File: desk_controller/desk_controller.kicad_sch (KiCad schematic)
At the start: 25 parts

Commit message: Some work
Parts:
- removed J?: RJ12, symbol Connector:RJ12
- added J?: UART2_header, Connector_PinHeader_2.54mm:PinHeader_1x04_P2.54mm_Vertical, symbol Connector_Generic:Conn_01x04
- added J?: RJ45, symbol Connector:RJ45
- added R? (x6): R, symbol Device:R
- added U? (x4): PC817, Package_DIP:DIP-4_W7.62mm, symbol Isolator:PC817
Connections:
- net +3V3: now also J?.1 (Pin_1), U?.4
- net GND: now also J?.4 (Pin_4), R?.1, R?.1, U?.2, U?.2, U?.2, U?.2
- net MISO: no longer names the net of U?.12 (PA6)
- net MOSI: no longer names the net of U?.13 (PA7)
- net NAND_CS: no longer names the net of U?.10 (PA4)
- net PA0: no longer names the net of U?.6 (PA0)
- net PA1: no longer names the net of U?.7 (PA1)
- net PA11: no longer names the net of U?.21 (PA11)
- net PA12: no longer names the net of U?.22 (PA12)
- net PA15: no longer names the net of U?.25 (PA15)
- net PA2: no longer names the net of U?.8 (PA2)
- net PA3: no longer names the net of U?.9 (PA3)
- net PA8: no longer names the net of U?.18 (PA8)
- net PB0: no longer names the net of U?.14 (PB0)
- net PB1: no longer names the net of U?.15 (PB1)
- net PB3: no longer names the net of U?.26 (PB3)
- net PB4: no longer names the net of U?.27 (PB4)
- net PB5: no longer names the net of U?.28 (PB5)
- net PB6: no longer names the net of U?.29 (PB6)
- net PB7: no longer names the net of U?.30 (PB7)
- net SCK: no longer names the net of U?.11 (PA5)
- new net: R?.2, U?.1 (x4)
- new net 232_RX: R?.1
- new net 232_RX_ISOLATED: R?.2, U?.3
- new net 232_TX: R?.1
- new net 232_TX_ISOLATED: R?.2, U?.3
- new net POWER_SIG: R?.1
- new net RESET_SIG: R?.1
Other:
- note added: "MJ3215-88-1-2-N"
- note added: "optos are APC-817D1-SL"
- company: (none) -> Stefano Nicolis
- title: (none) -> Desk Controller
- moved on the sheet: C?, D?, J?, PS?, Q?, R?, RV?, SW?, U?

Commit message: Sch work
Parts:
- added C?: 10u, symbol Device:C_Polarized
- added D?: D_Schottky, symbol Device:D_Schottky
- added R?: R, symbol Device:R
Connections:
- net 232_RX: now also J?.6
- net 232_TX: now also J?.5
- net GND: now also J?.8, C?.2
- net VBUS: now reaches U?.4
- net VBUS: now also C?.1, R?.1
- net POWER-: now reaches U?.3
- net POWER-: now also J?.2
- net POWER+: now reaches U?.4
- net POWER+: now also J?.1
- net RESET-: now reaches U?.3
- net RESET-: now also J?.4
- net RESET+: now reaches U?.4
- net RESET+: now also J?.3
- net 232_DTR: now reaches J?.7
- net 232_DTR: now also D?.2 (A)
- new net: D?.1 (K), R?.2
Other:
- moved on the sheet: C?, D?, J?, PS?, Q?, R?, RV?, SW?, U?

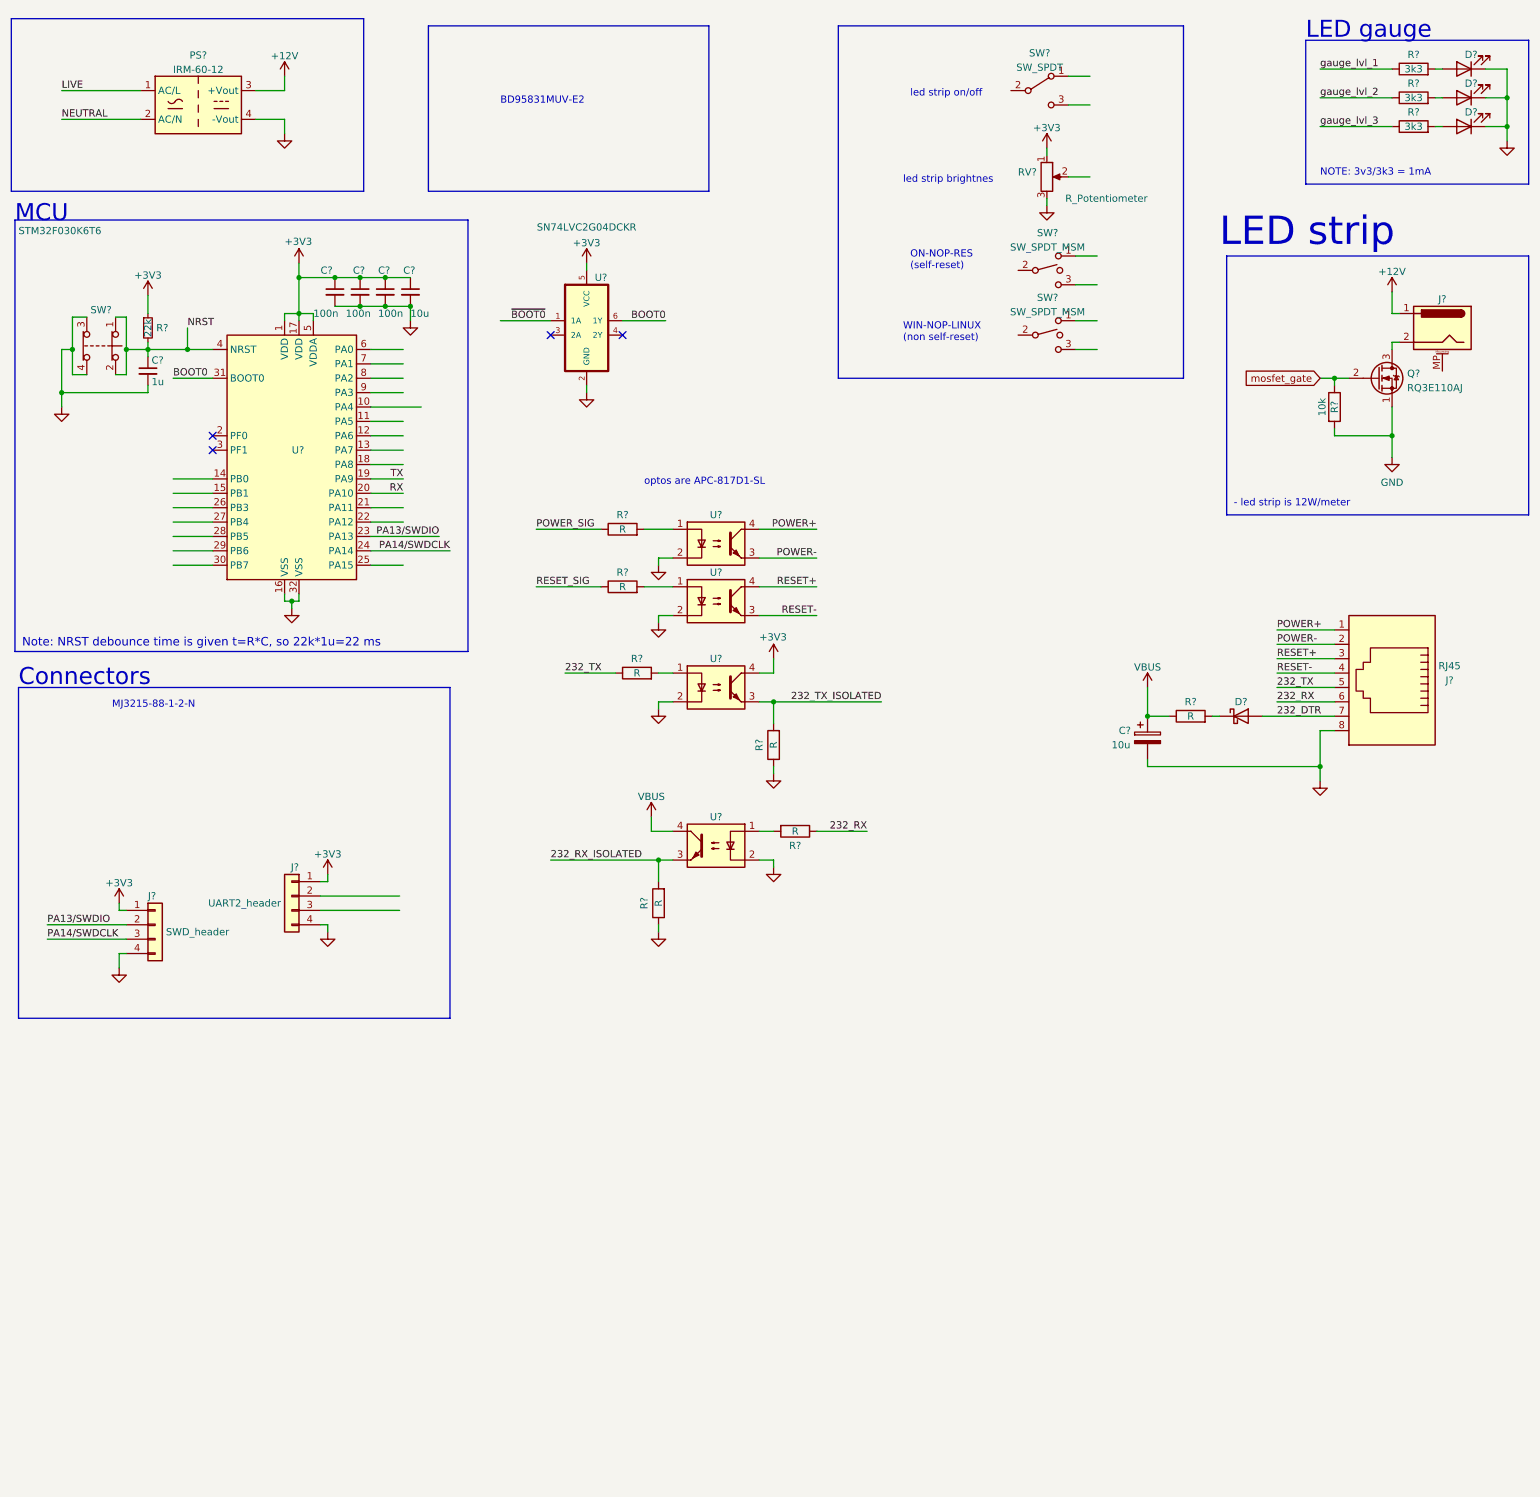
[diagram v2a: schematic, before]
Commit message: Added sheets in sch, added TI document for isolated rs232 interface with power harvesting, general sch work
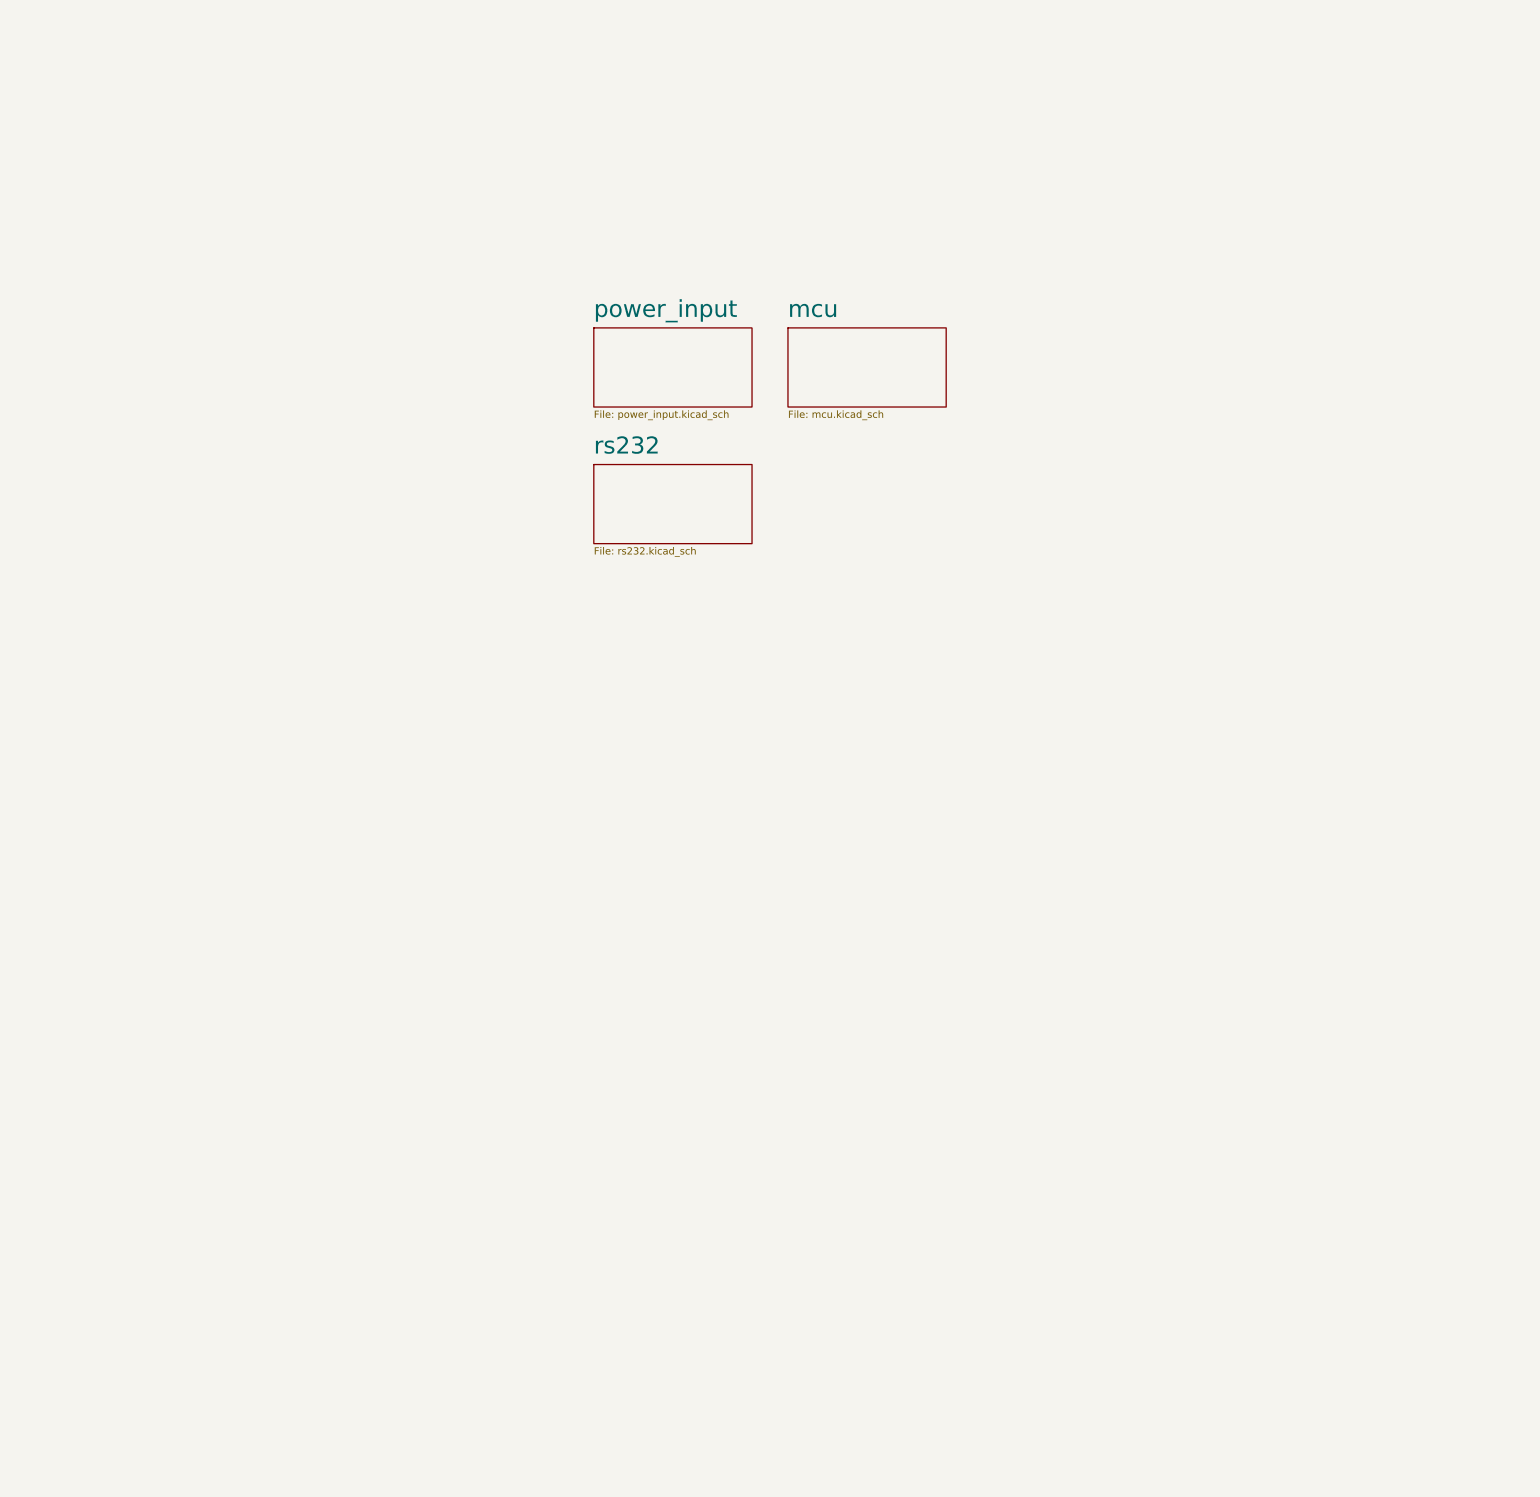
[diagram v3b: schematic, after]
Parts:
- removed C?: 1u, Capacitor_SMD:C_0603_1608Metric, symbol Device:C_Small
- removed C? (x3): 100n, Capacitor_SMD:C_0603_1608Metric, symbol Device:C_Small
- removed C?: 10u, symbol Device:C_Polarized
- removed C?: 10u, Capacitor_SMD:C_0603_1608Metric, symbol Device:C_Small
- removed D?: GREEN, LED_SMD:LED_0603_1608Metric, symbol Device:LED
- removed D? (x2): RED, LED_SMD:LED_0603_1608Metric, symbol Device:LED
- removed D?: D_Schottky, symbol Device:D_Schottky
- removed J?: UART2_header, Connector_PinHeader_2.54mm:PinHeader_1x04_P2.54mm_Vertical, symbol Connector_Generic:Conn_01x04
- removed J?: SWD_header, Connector_PinHeader_2.54mm:PinHeader_1x04_P2.54mm_Vertical, symbol Connector_Generic:Conn_01x04
- removed J?: Barrel_Jack_MountingPin, symbol Connector:Barrel_Jack_MountingPin
- removed J?: RJ45, symbol Connector:RJ45
- removed PS?: IRM-60-12, Converter_ACDC:Converter_ACDC_MeanWell_IRM-60-xx_THT, symbol Converter_ACDC:IRM-60-12
- removed Q?: RQ3E110AJ, SOTFL65P330X80-8N:SOTFL65P330X80-8N, symbol RQ3E100GNTB:RQ3E110AJ
- removed R? (x3): 3k3, Resistor_SMD:R_0603_1608Metric, symbol Device:R
- removed R? (x7): R, symbol Device:R
- removed R?: 22k, Resistor_SMD:R_0603_1608Metric, symbol Device:R_Small
- removed R?: 10k, Resistor_SMD:R_0603_1608Metric, symbol Device:R
- removed RV?: R_Potentiometer, symbol Device:R_Potentiometer
- removed SW?: SW_Push_Open_Dual, SKRPACE010:SW_SKRPACE010, symbol Switch:SW_Push_Open_Dual
- removed SW? (x2): SW_SPDT_MSM, symbol Switch:SW_SPDT_MSM
- removed SW?: SW_SPDT, symbol Switch:SW_SPDT
- removed U? (x4): PC817, Package_DIP:DIP-4_W7.62mm, symbol Isolator:PC817
- removed U?: SN74LVC2G04DCKR, SN74LVC2G04DCKR:SOT65P210X110-6N, symbol SN74LVC2G04DCKR:SN74LVC2G04DCKR
- removed U?: STM32F030K6T6, Package_QFP:LQFP-32_7x7mm_P0.8mm, symbol MCU_ST_STM32F0:STM32F030K6Tx
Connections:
- no-connect marks 4 -> 0
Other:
- added sheet mcu (mcu.kicad_sch)
- added sheet power_input (power_input.kicad_sch)
- added sheet rs232 (rs232.kicad_sch)
- note removed: "- led strip is 12W/meter"
- note removed: "BD95831MUV-E2"
- note removed: "Connectors"
- note removed: "LED gauge"
- note removed: "LED strip"
- note removed: "MCU"
- note removed: "MJ3215-88-1-2-N"
- note removed: "NOTE: 3v3/3k3 = 1mA"
- note removed: "Note: NRST debounce time is given t=R*C, so 22k*1u=22 ms"
- note removed: "ON-NOP-RES (self-reset)"
- note removed: "WIN-NOP-LINUX (non self-reset)"
- note removed: "led strip brightnes"
- note removed: "led strip on/off"
- note removed: "optos are APC-817D1-SL"

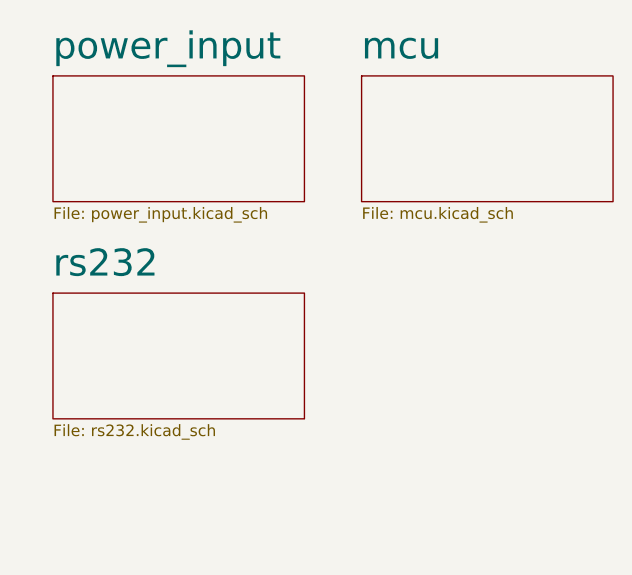
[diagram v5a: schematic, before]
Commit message: Buck converter sch, rs232 transceiver
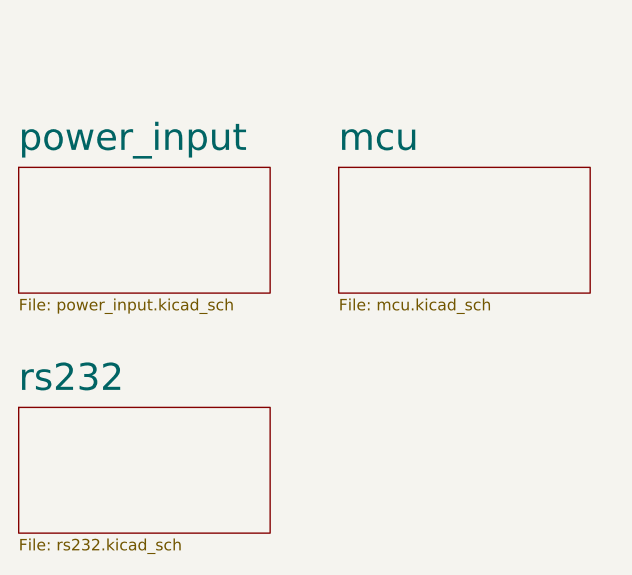
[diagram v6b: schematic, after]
